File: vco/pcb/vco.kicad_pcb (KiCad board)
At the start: 2 copper layers, 50.5 x 108.5 mm, 100 parts, among them J1 Conn_02x05_Odd_Even, J10 AudioJack2_SwitchT, J2 AudioJack2_SwitchT, J3 AudioJack2_SwitchT, J4 AudioJack2_SwitchT, J5 AudioJack2_SwitchT, J6 AudioJack2_SwitchT, J7 AudioJack2_SwitchT, J8 AudioJack2_SwitchT, J9 AudioJack2_SwitchT, Q1 DMMT3906W, Q2 BC847, SW1 SW_SPDT, SW2 SW_SPDT, U1 TL072, U2 TL074, U3 LM13700, U4 ICM7555xB, U5 TL074

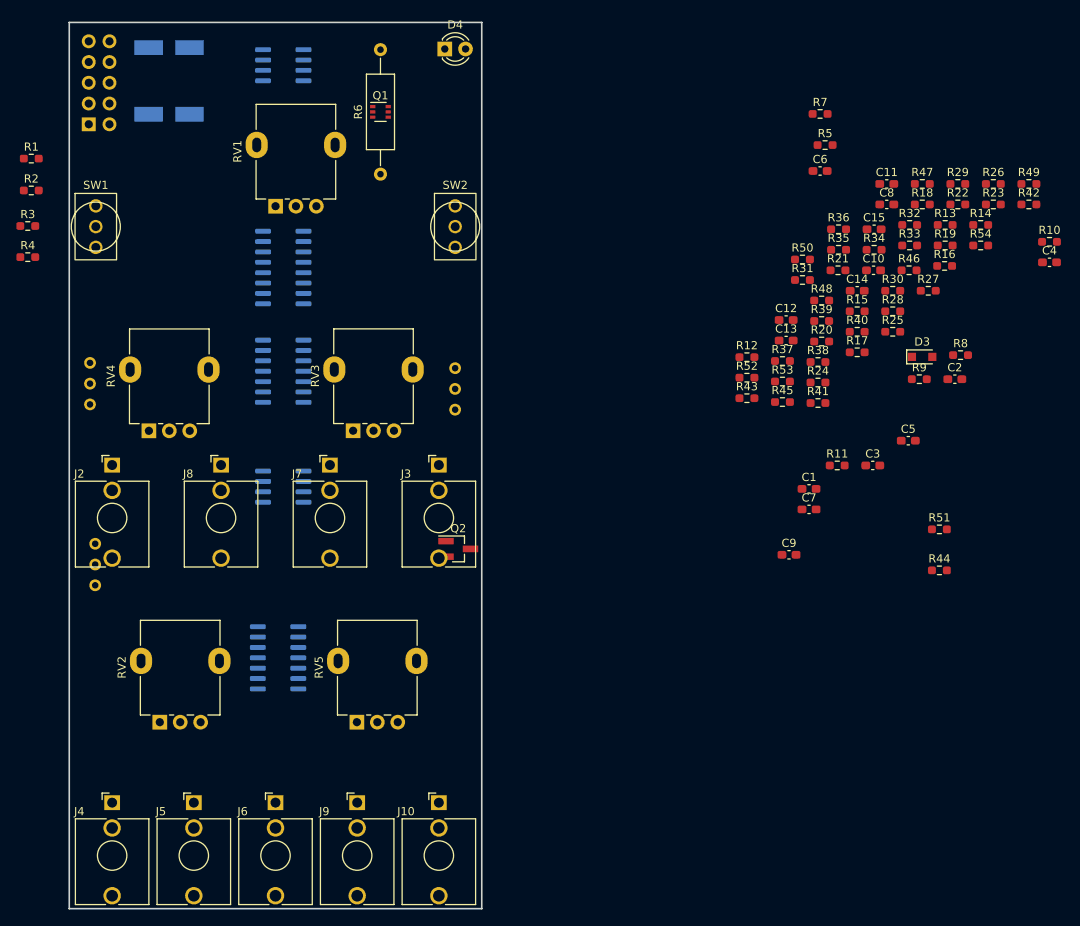
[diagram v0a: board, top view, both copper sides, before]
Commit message: vco: Layout WIP: component placement
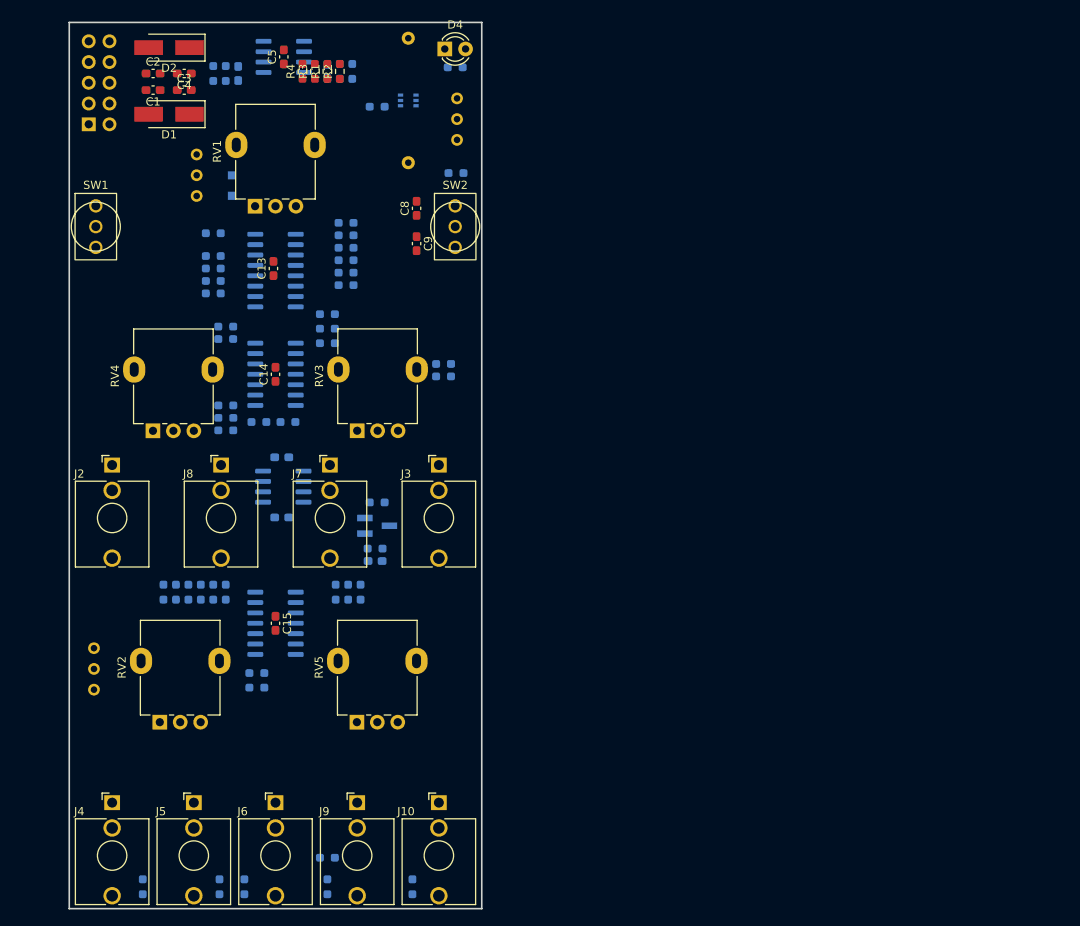
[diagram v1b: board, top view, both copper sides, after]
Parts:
- C10, C11, C12, C6, C7, Q1, Q2, R10, R11, R12, R13, R14, R15, R16, R17, R18, R19, R20, R21, R22, R23, R24, R25, R26, R27, R28, R29, R30, R31, R32, R33, R34, R35, R36, R37, R38, R39, R40, R41, R42, R43, R44, R45, R46, R47, R48, R49, R5, R50, R51, R52, R53, R54, R6, R7, R8, R9: moved to B.Cu
- D1, D2: moved to F.Cu
- D3: value D -> 1N4148; moved to B.Cu
- moved R22 120.9 mm to (-3.81, 115.6), turned to -90 degrees
- moved R49 112.9 mm to (-2.29, 91.2)
- moved C4 108.4 mm to (-11.2, 16.0), turned to 180 degrees
- moved R33 106.0 mm to (6.35, 115.6), turned to 90 degrees
- moved R32 105.3 mm to (6.35, 112.0)
- moved C2 105.0 mm to (-15.0, 16.0)
- moved R47 102.8 mm to (-10.7, 79.5), turned to -90 degrees
- moved R53 99.8 mm to (-16.3, 115.6), turned to -90 degrees
- moved R42 97.2 mm to (7.37, 79.5), turned to -90 degrees
- moved C3 96.0 mm to (-11.2, 18.0)
- moved R46 95.2 mm to (-9.14, 79.5), turned to 90 degrees
- moved R44 95.0 mm to (-13.7, 79.5), turned to 90 degrees
- moved R14 94.3 mm to (-7.62, 42.9)
- moved C1 94.0 mm to (-15.0, 18.0), turned to 180 degrees
- moved R23 93.8 mm to (-2.03, 58.7)
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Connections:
- SW1 pad 1: EFM -> LFM
- SW1 pad 3: LFM -> EFM
- U5 pad 1: Net-(R46-Pad2) -> Net-(R51-Pad2)
- U5 pad 13: Net-(R49-Pad2) -> Net-(R43-Pad2)
- U5 pad 14: Net-(R51-Pad2) -> Net-(R46-Pad2)
- U5 pad 2: Net-(R43-Pad2) -> Net-(R49-Pad2)

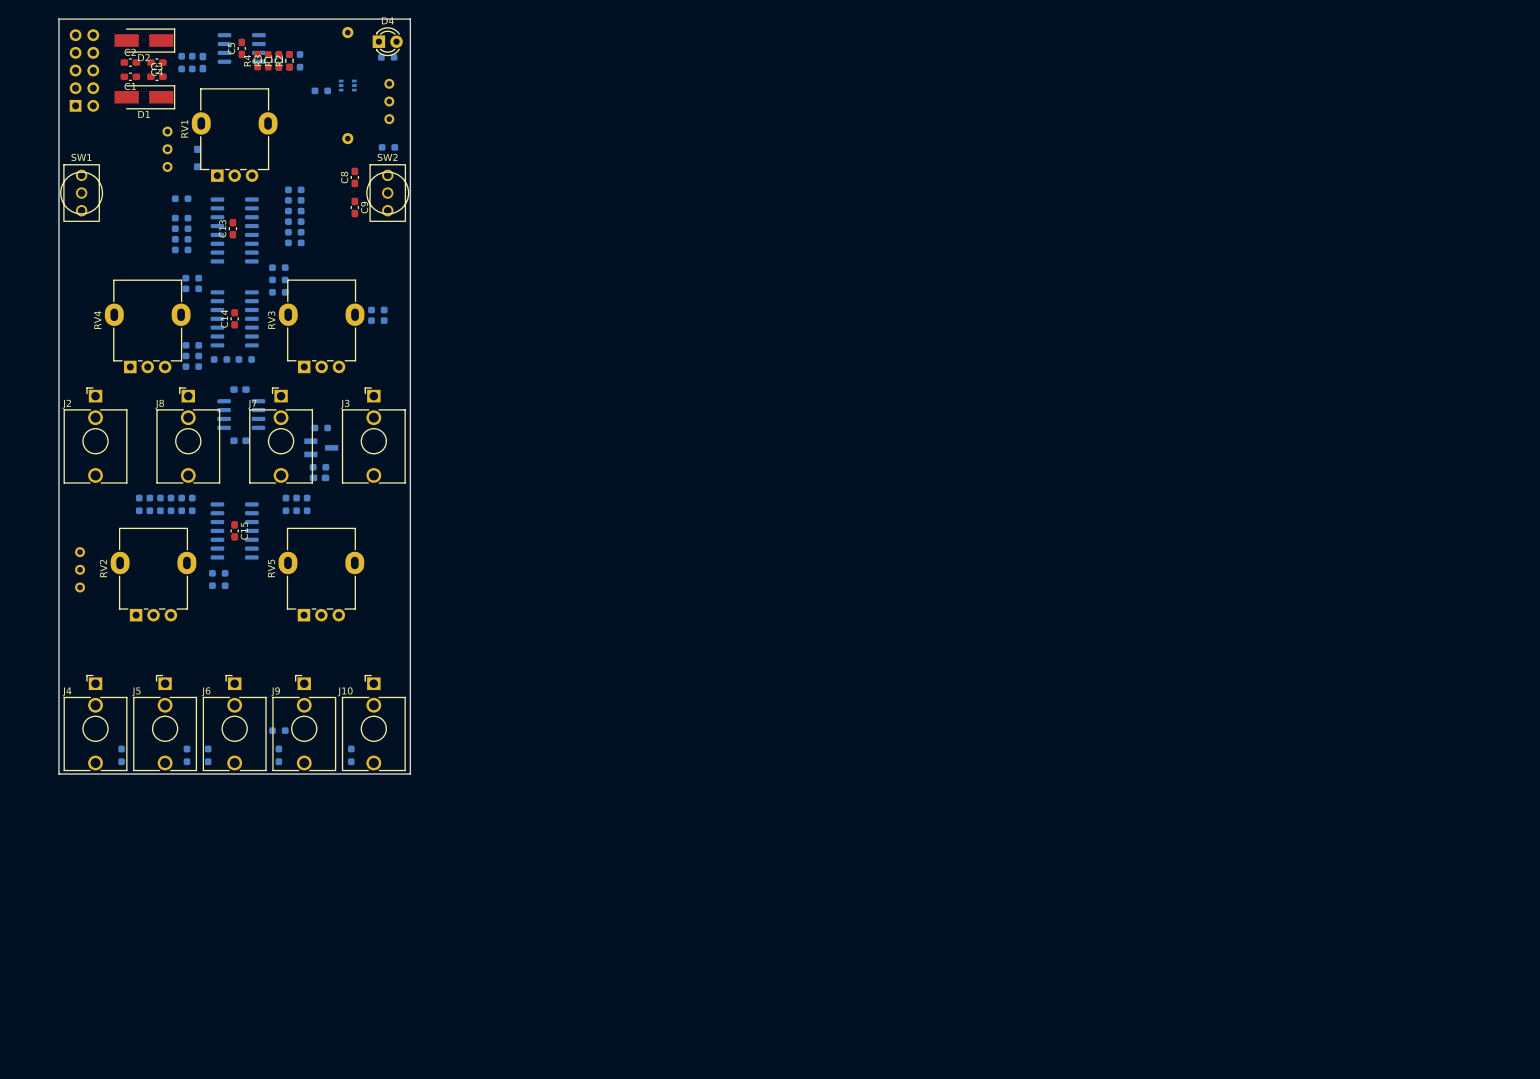
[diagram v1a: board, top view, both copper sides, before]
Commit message: vco: Layout
Silkscreen still needs adjustment.
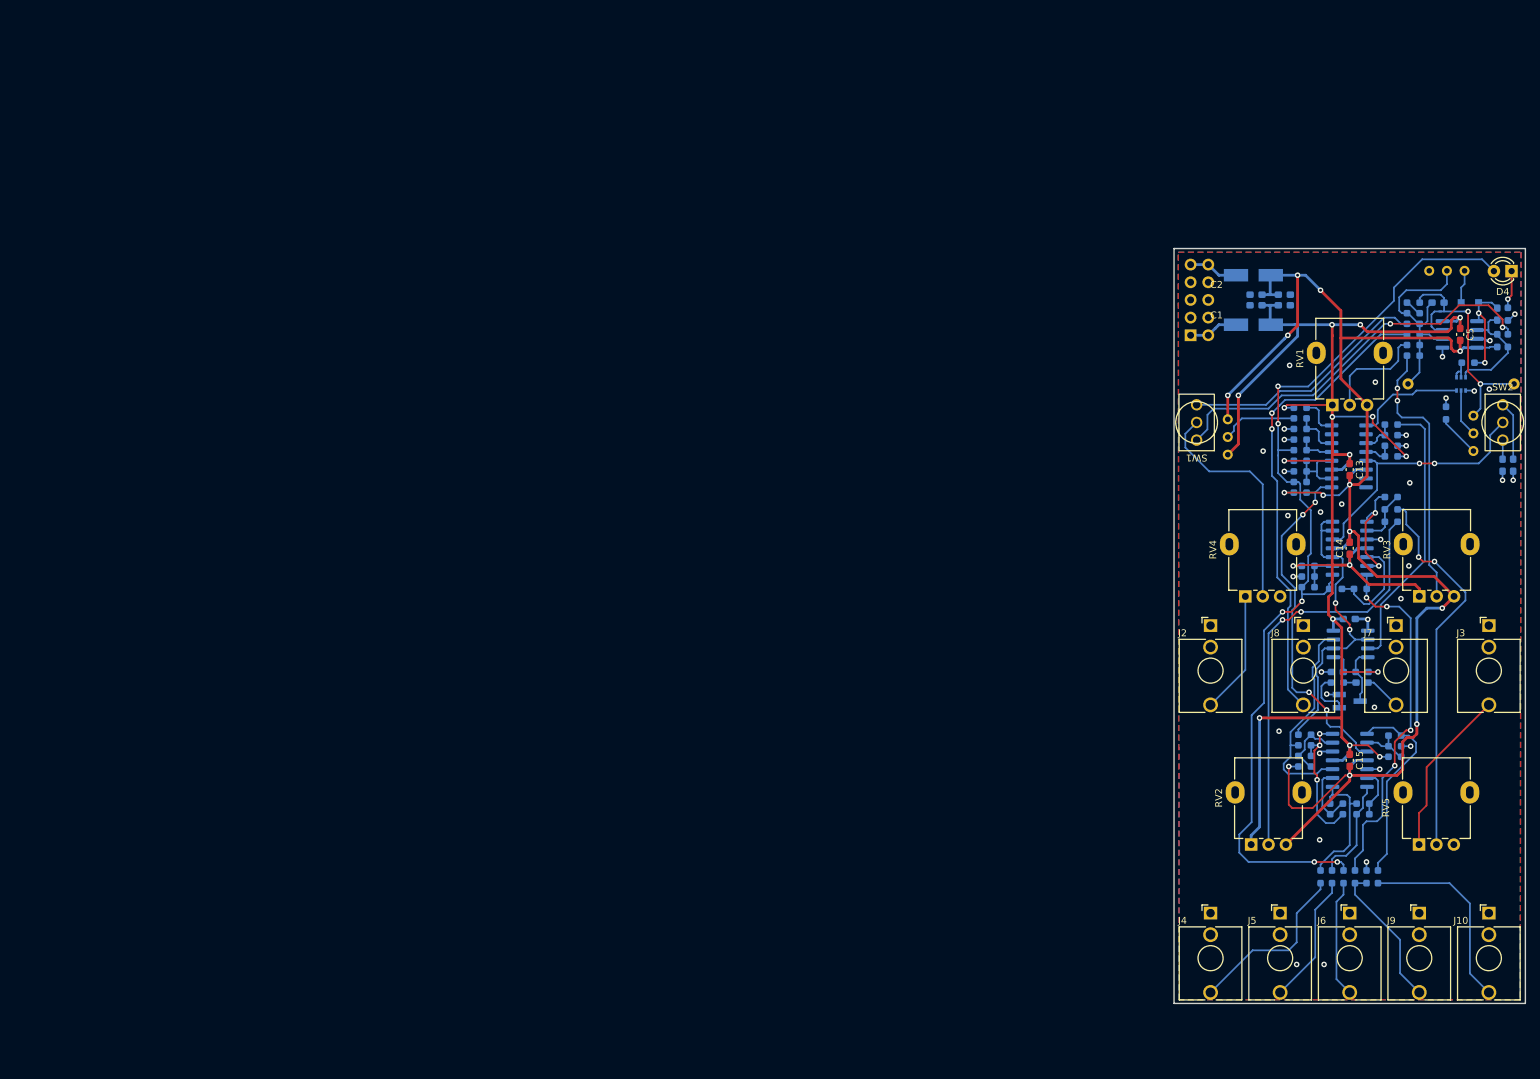
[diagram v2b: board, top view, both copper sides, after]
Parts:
- removed R25, R30: 0R, Resistor_SMD:R_0603_1608Metric_Pad0.98x0.95mm_HandSolder
- C1, C2, C3, C4, C8, C9, D1, D2, R1, R2, R3, R4: moved to B.Cu
- moved R11 193.3 mm to (181.5, 56.0)
- moved R9 193.3 mm to (183.0, 56.0), turned to -90 degrees
- moved C7 189.5 mm to (181.5, 52.2), turned to 90 degrees
- moved RV7 187.0 mm to (176.8, 45.9), turned to 0 degrees
- moved D3 184.0 mm to (177.5, 50.5), turned to 0 degrees
- moved C5 179.9 mm to (176.1, 55.1), turned to -90 degrees
- moved U1 179.8 mm to (176.1, 55.1), turned to 180 degrees
- moved R19 177.2 mm to (166.2, 72.6), turned to 180 degrees
- moved R20 176.6 mm to (166.2, 71.1), turned to 0 degrees
- moved R18 176.1 mm to (166.2, 69.5), turned to 180 degrees
- moved R14 175.7 mm to (166.2, 68.0), turned to 180 degrees
- moved R53 173.2 mm to (156.1, 133.0)
- moved R48 171.9 mm to (158.4, 124.0), turned to 180 degrees
- moved R44 171.7 mm to (153.8, 117.2), turned to 0 degrees
- moved C8 171.5 mm to (183.8, 73.9)
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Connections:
- R43 pad 1: Net-(R30-Pad2) -> Net-(U2-Pad13)
- SW2 pad 2: Net-(R25-Pad1) -> Net-(U2-Pad12)
- U2 pad 10: Net-(R30-Pad2) -> Net-(U2-Pad13)
- U2 pad 12: Net-(R25-Pad2) -> Net-(U2-Pad12)
- U2 pad 13: Net-(R30-Pad1) -> Net-(U2-Pad13)
- U2 pad 14: Net-(R30-Pad2) -> Net-(U2-Pad13)
- U3 pad 10: unconnected-(U3-Pad10) -> Net-(R35-Pad2)
- U3 pad 5: Net-(R25-Pad1) -> Net-(U2-Pad12)
- U3 pad 7: Net-(R35-Pad2) -> unconnected-(U3-Pad7)
- U3 pad 8: Net-(R39-Pad2) -> unconnected-(U3-Pad8)
- U3 pad 9: unconnected-(U3-Pad9) -> Net-(R39-Pad2)
- U4 pad 2: Net-(R30-Pad2) -> Net-(U2-Pad13)
- U4 pad 6: Net-(R30-Pad2) -> Net-(U2-Pad13)
- U5 pad 1: Net-(R51-Pad2) -> Net-(R49-Pad1)
- U5 pad 13: Net-(R43-Pad2) -> Net-(R49-Pad2)
- U5 pad 14: Net-(R46-Pad2) -> Net-(R51-Pad2)
- U5 pad 2: Net-(R49-Pad2) -> Net-(R48-Pad2)
- U5 pad 3: GND -> Net-(R47-Pad2)
- U5 pad 5: Net-(R47-Pad2) -> GND
- U5 pad 6: Net-(R48-Pad2) -> Net-(R43-Pad2)
- U5 pad 7: Net-(R49-Pad1) -> Net-(R46-Pad2)
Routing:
- net +12V: track 0.00 -> 245.4 mm, vias 0 -> 17
- net -12V: track 0.00 -> 221.4 mm, vias 0 -> 13
- net Net-(D4-Pad2): track 0.00 -> 140.7 mm, vias 0 -> 6
- net CVJack: track 0.00 -> 68.2 mm, vias 0 -> 2
- net PWPot: track 0.00 -> 60.6 mm, vias 0 -> 2
- net LFM: track 0.00 -> 56.8 mm, vias 0 -> 2
- net PWCVPot: track 0.00 -> 55.4 mm, vias 0 -> 2
- net Net-(R24-Pad2): track 0.00 -> 51.7 mm, vias 0 -> 4
- net Net-(R39-Pad2): track 0.00 -> 51.0 mm, vias 0 -> 4
- net Net-(U2-Pad13): track 0.00 -> 45.0 mm, vias 0 -> 2
- net Net-(R14-Pad1): track 0.00 -> 39.9 mm
- net FFPot: track 0.00 -> 39.3 mm, vias 0 -> 2
- net Net-(U2-Pad12): track 0.00 -> 38.0 mm, vias 0 -> 2
- net Net-(C6-Pad2): track 0.00 -> 36.9 mm, vias 0 -> 2
- net EFM: track 0.00 -> 35.8 mm
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- added copper zone on B.Cu, net GND
- added copper zone on F.Cu, net GND

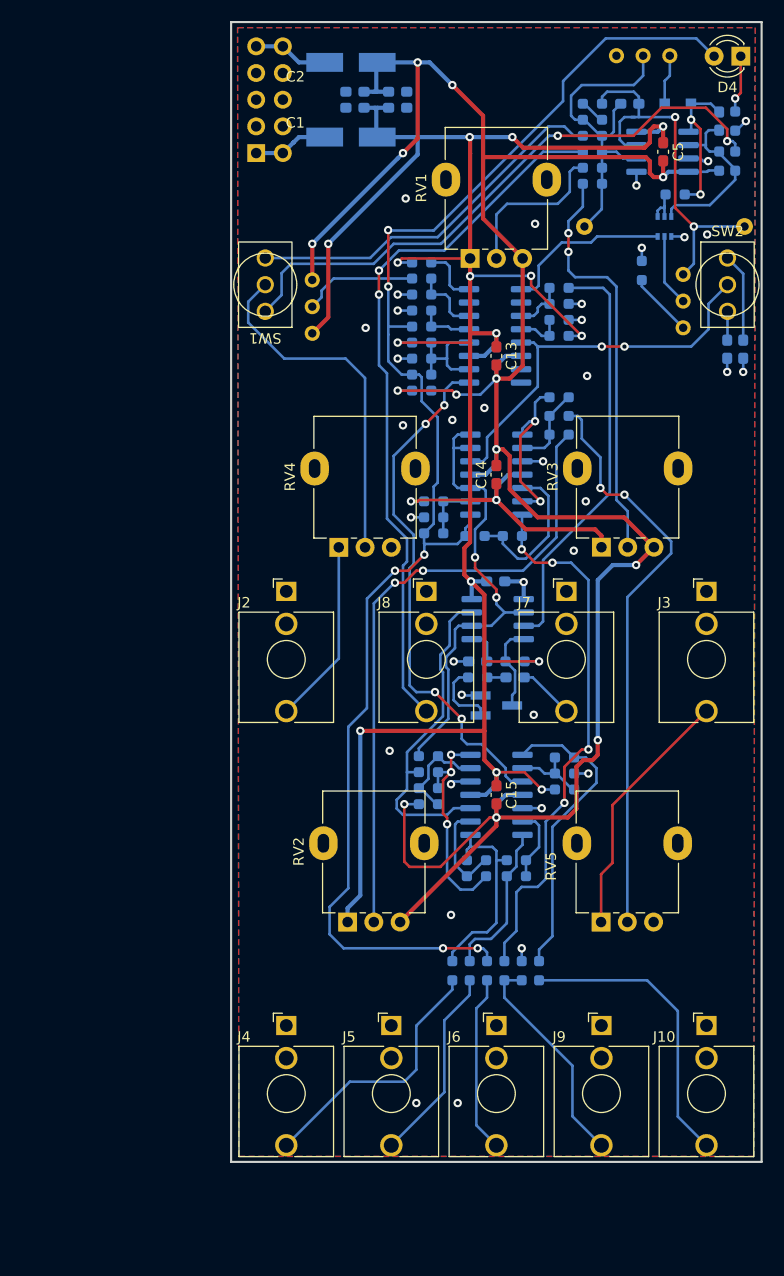
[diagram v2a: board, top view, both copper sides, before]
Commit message: vco: Layout fixes and dimensions
Fixed the location of two pots and added dimensions to aid in front
panel design.
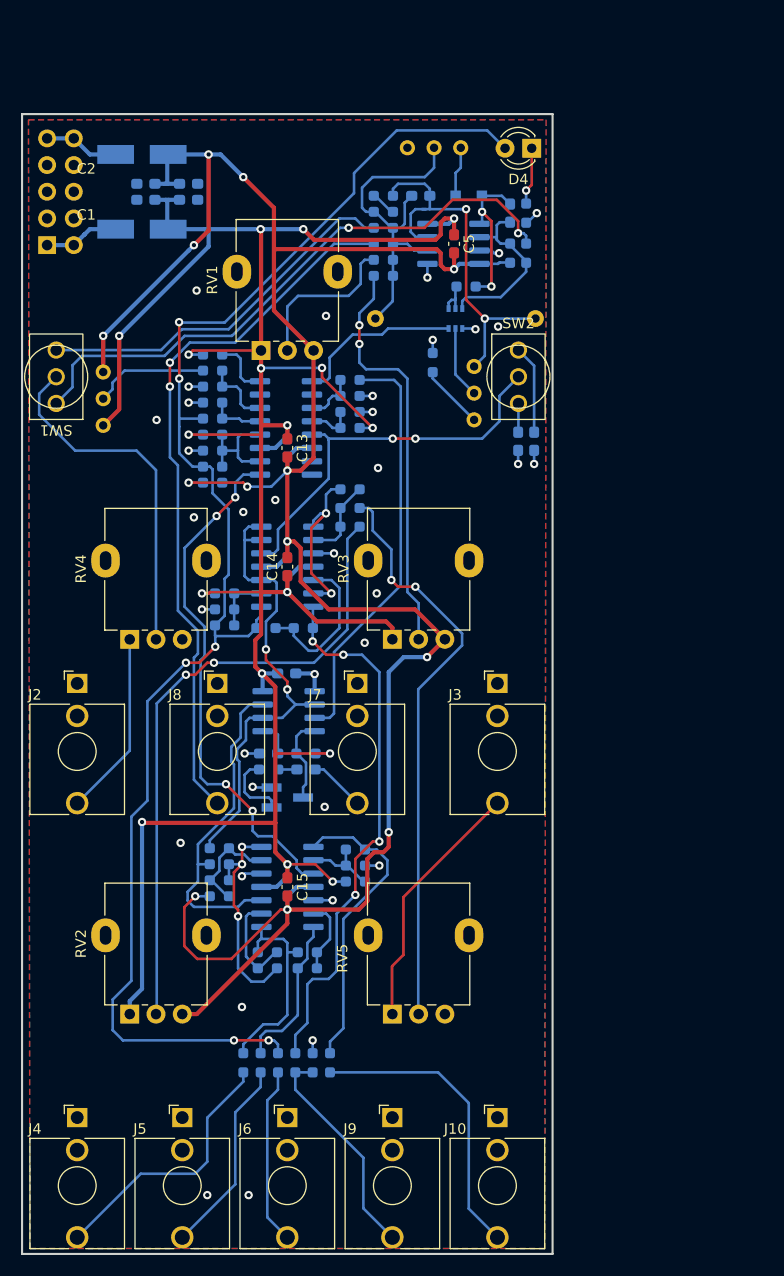
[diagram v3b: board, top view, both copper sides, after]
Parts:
- moved RV2 22.5 mm to (125.4, 137.2)
- moved C1 21.7 mm to (131.0, 59.6)
- moved C14 21.7 mm to (140.4, 94.6)
- moved C6 21.7 mm to (153.1, 59.3)
- moved C9 21.7 mm to (162.3, 82.6)
- moved D3 21.7 mm to (157.6, 59.3)
- moved J10 21.7 mm to (160.4, 147.0)
- moved J4 21.7 mm to (120.4, 147.0)
- moved J5 21.7 mm to (130.4, 147.0)
- moved J6 21.7 mm to (140.4, 147.0)
- moved J9 21.7 mm to (150.4, 147.0)
- moved R10 21.7 mm to (157.4, 67.9)
- moved R14 21.7 mm to (146.3, 76.8)
- moved R15 21.7 mm to (146.3, 90.8)
- moved R16 21.7 mm to (146.3, 89.0)
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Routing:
- net -12V: track 221.4 -> 223.6 mm
- net Net-(D4-Pad2): track 140.7 -> 141.9 mm
- net +12V: track 245.4 -> 246.3 mm
